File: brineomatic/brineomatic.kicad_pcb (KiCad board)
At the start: 4 copper layers, 106 x 66.5 mm, 171 parts, among them J1 Conn_01x04_MountingPin, J10 5.08MM, J12 3.5MM, J14 3.5MM, J16 3.5MM, J19 USB_TYPE_C_16PIN, J21 Conn_01x04, J7 3.5MM, Q1 AO3400A, Q2 AO3400A, Q3 20N06, Q4 AO3400A, Q5 AO3400A, Q6 AO3400A, Q7 FDC6330L, Q8 S8050, Q9 S8050, SW1 RESET, SW2 BOOT, U1 ADS1115IDGSR, U2 LM74700, U3 XL1509-5.0, U4 ESP32-S3-WROOM-1-N16R8, U5 USBLC6-2SC6, U6 XC6210B332MR, U7 CH334F, U8 CH343P, U9 TMC2209-LA, Y1 12Mhz, Y2 32.768kHz

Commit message: added rs485 circuit
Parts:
- added C45: 10uF, Capacitor_SMD:C_0603_1608Metric, F.Cu at (109.6, 117.1)
- added C46: 100nF, Capacitor_SMD:C_0603_1608Metric, F.Cu at (109.6, 114.6)
- added J22: 3.5mm, Connector_Phoenix_MC:PhoenixContact_MC_1,5_3-G-3.5_1x03_P3.50mm_Horizontal, F.Cu at (111.0, 120.9)
- added R53: 10k, Resistor_SMD:R_0603_1608Metric, F.Cu at (109.6, 112.1)
- added R54: 10k, Resistor_SMD:R_0603_1608Metric, F.Cu at (109.6, 109.6)
- added R55: 10k, Resistor_SMD:R_0603_1608Metric, F.Cu at (114.2, 109.3)
- added R56: 10k, Resistor_SMD:R_0603_1608Metric, F.Cu at (119.0, 109.6)
- added R57: 10k, Resistor_SMD:R_0603_1608Metric, F.Cu at (119.0, 112.1)
- added R58: 120R, Resistor_SMD:R_0603_1608Metric, F.Cu at (119.0, 114.6)
- added R59: 10k, Resistor_SMD:R_0603_1608Metric, F.Cu at (119.0, 117.1)
- added U10: MAX3485, Package_SO:SOIC-8_3.9x4.9mm_P1.27mm, F.Cu at (114.3, 114.1)
- renumbered D11 to D10, D10 to D11
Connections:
- U4 pad 24: /ESP32-S3/GPIO47 -> GPIO47
- U4 pad 25: /ESP32-S3/GPIO48 -> GPIO48
- U4 pad 5: /ESP32-S3/GPIO5 -> GPIO5

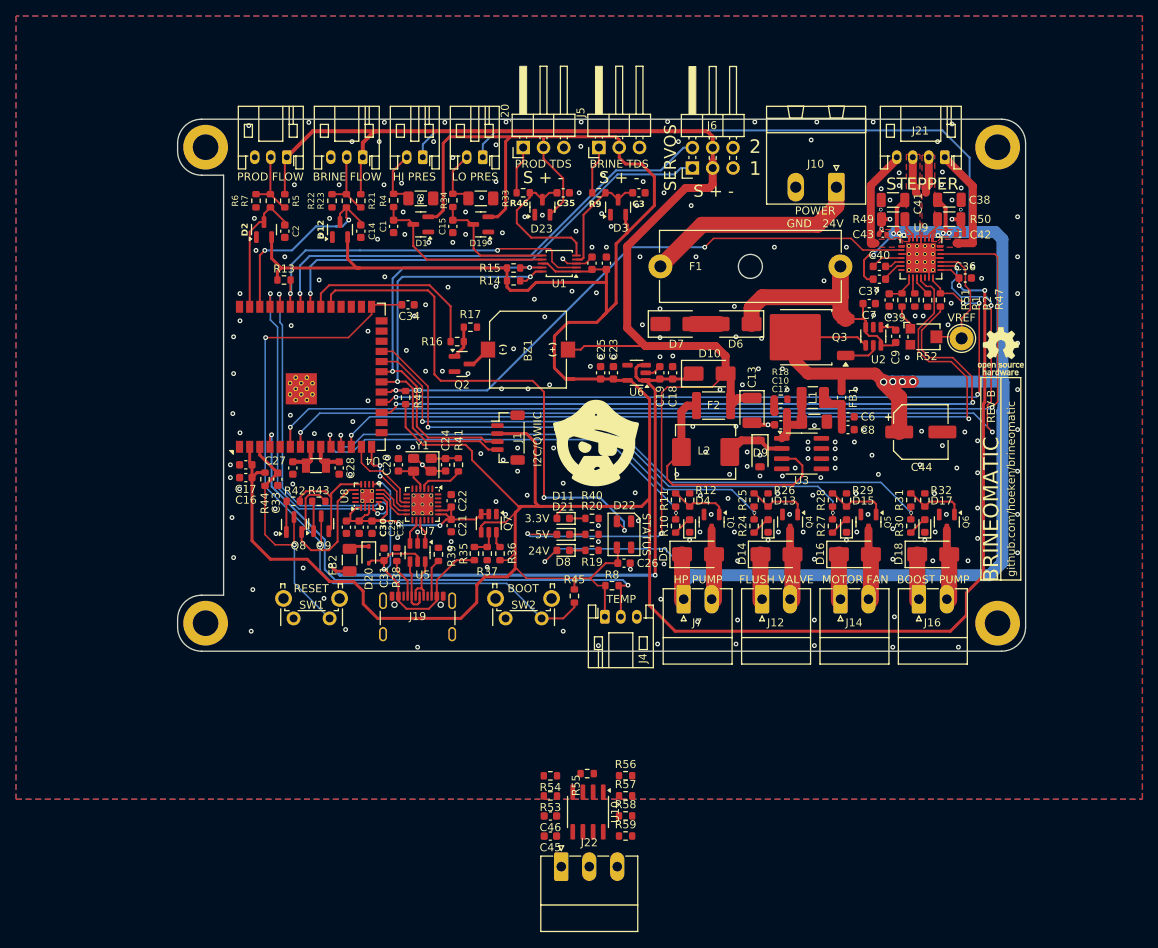
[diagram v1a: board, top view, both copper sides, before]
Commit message: stacked tds, removed stepper vref, pulled in esp32-s3 schematic, added extra relay output
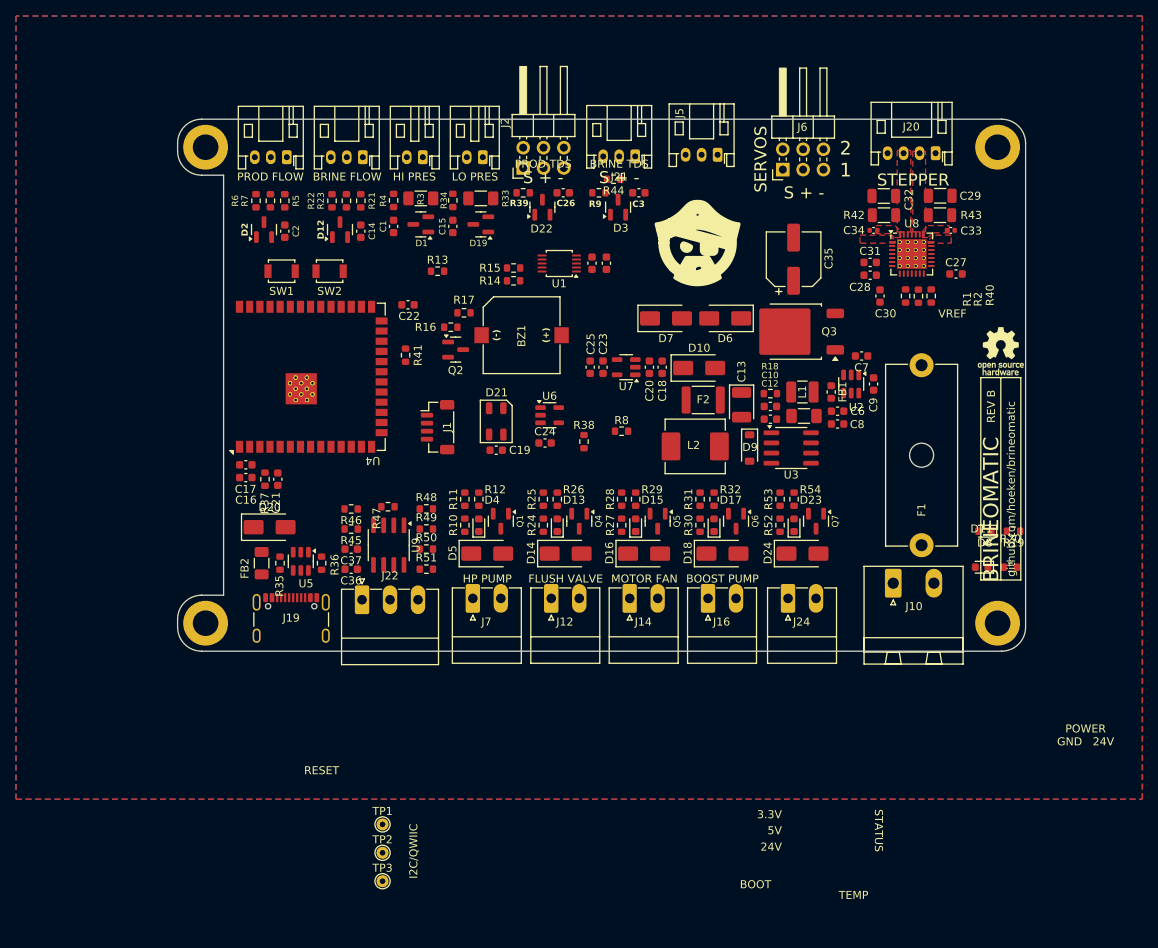
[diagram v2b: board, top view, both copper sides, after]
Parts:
- removed the C20 at (90.6, 70.7)
- removed the C21 at (97.2, 78.3)
- removed the C22 at (97.2, 75.2)
- removed the C27 at (77.4, 71.1)
- removed the C28 at (83.2, 71.1)
- removed the C29 at (85.7, 78.5)
- removed the C30 at (84.1, 78.5)
- removed the C31 at (88.8, 81.9)
- removed the C32 at (87.3, 78.5)
- removed the D21 at (111.2, 77.4)
- removed the J20 at (106.2, 31.0)
- removed the J5 at (115.7, 31.0)
- removed Q8, Q9: S8050, Package_TO_SOT_SMD:SOT-23
- removed the R35 at (100.1, 81.8)
- removed the R36 at (103.3, 81.8)
- removed the R37 at (101.7, 81.8)
- removed the R40 at (114.8, 77.4)
- removed the R41 at (98.1, 70.7)
- removed the R42 at (77.5, 75.3)
- removed the R43 at (80.7, 75.3)
- removed the R51 at (153.6, 50.1)
- removed the U7 at (93.6, 75.7)
- removed the U8 at (86.7, 74.6)
- removed Y1: 12Mhz, Crystal:Crystal_SMD_SeikoEpson_TSX3225-4Pin_3.2x2.5mm
- removed Y2: 32.768kHz, Crystal:Crystal_SMD_3215-2Pin_3.2x1.5mm
- added D23: RED, LED_SMD:LED_0603_1608Metric, F.Cu at (140.1, 78.2)
- added D24: SS54, Diode_SMD:D_SMA, F.Cu at (141.1, 81.8)
- added J2: ~, Connector_PinHeader_2.54mm:PinHeader_2x03_P2.54mm_Horizontal, F.Cu at (106.2, 33.6)
- added J21: ~, Connector_JST:JST_PH_S3B-PH-K_1x03_P2.00mm_Horizontal, F.Cu at (120.2, 32.1)
- added J24: 3.5MM, yarrboard:PhoenixContact_MC_1,5_2-G-3.5_1x02_P3.50mm_Horizontal, F.Cu at (139.3, 87.4)
- added R44: 4.7K, Resistor_SMD:R_0603_1608Metric, F.Cu at (117.5, 35.0)
- added R53: 100R, Resistor_SMD:R_0603_1608Metric, F.Cu at (138.3, 75.0)
- added R54: 10k, Resistor_SMD:R_0603_1608Metric, F.Cu at (140.1, 75.0)
- added TP2: ~, TestPoint:TestPoint_THTPad_D1.5mm_Drill0.7mm, F.Cu at (88.6, 119.2)
- added TP3: ~, TestPoint:TestPoint_THTPad_D1.5mm_Drill0.7mm, F.Cu at (88.6, 122.8)
- added U6: SN74LV1T34DBV, Package_TO_SOT_SMD:SOT-23-5, F.Cu at (109.5, 64.5)
- C24: value 15pF -> 100nF
- D20: value 1N5819WS -> SS36; footprint Diode_SMD:D_SOD-323 -> Diode_SMD:D_SMA
- FB2: value 1.5A -> 4A
- Q7: value FDC6330L -> AO3400A; footprint Package_TO_SOT_SMD:TSOT-23-6 -> Package_TO_SOT_SMD:SOT-23
- R52: value 20k -> 1k; footprint Potentiometer_SMD:Potentiometer_Bourns_TC33X_Vertical -> Resistor_SMD:R_0603_1608Metric
- SW1, SW2: footprint Button_Switch_THT:SW_Tactile_SPST_Angled_PTS645Vx58-2LFS -> Button_Switch_SMD:SW_SPST_B3U-1000P
- TP1: value TestPoint -> ~; footprint TestPoint:TestPoint_THTPad_D3.0mm_Drill1.5mm -> TestPoint:TestPoint_THTPad_D1.5mm_Drill0.7mm
- moved TP1 94.5 mm to (88.6, 115.7), turned to 0 degrees
- moved J5 59.4 mm to (130.5, 31.9), turned to 180 degrees
- moved D8 52.8 mm to (163.9, 79.0)
- moved R19 52.8 mm to (167.5, 79.0)
- moved D11 52.5 mm to (163.5, 83.5)
- moved R20 52.5 mm to (167.1, 83.5)
- moved SW2 50.9 mm to (82.0, 46.5)
- moved J10 50.0 mm to (152.5, 85.5), turned to 0 degrees
- moved F1 47.8 mm to (156.0, 80.8), turned to 90 degrees
- moved SW1 43.8 mm to (76.0, 46.5)
- moved C36 41.6 mm to (84.7, 83.8)
- moved R45 41.6 mm to (84.7, 78.7)
- moved R46 41.6 mm to (84.7, 76.2)
- moved R47 41.6 mm to (89.3, 75.9)
- moved R49 41.6 mm to (94.1, 78.7)
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- renumbered C26 to C19, C19 to C20, C33 to C21, C34 to C22, C35 to C26, C36 to C27, C37 to C28, C38 to C29, C39 to C30, C40 to C31, C41 to C32, C42 to C33, C43 to C34, C44 to C35, C45 to C36, C46 to C37, D22 to D21, D23 to D22, J21 to J20, J2 to J3, J3 to J4, J4 to J5, R38 to R35, R39 to R36, R44 to R37, R45 to R38, R46 to R39, R47 to R40, R48 to R41, R49 to R42, R50 to R43, R53 to R45, R54 to R46, R55 to R47, R56 to R48, R57 to R49, R58 to R50, R59 to R51, U6 to U7, U9 to U8, U10 to U9
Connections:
- net ADC_ALERT/RDY renamed ADC_ALERT
- C13 pad 1: Net-(D10-A) -> 5V_TRUE
- C18 pad 1: ESP32_5V -> +5V
- C19 pad 1: +3.3V -> +5V
- C20 pad 1: ESP32_5V -> +5V
- C24 pad 1: Net-(C24-Pad1) -> +5V
- D10 pad 2: Net-(D10-A) -> 5V_TRUE
- D21 pad 1: +3.3V -> +5V
- D21 pad 4: /ESP32-S3/GPIO38 -> Net-(D21-DIN)
- F2 pad 1: Net-(D10-A) -> 5V_TRUE
- FB2 pad 2: ESP32_5V -> +5V
- J11 pad 1: +5V -> 5V_TRUE
- J4 pad 1: +5V -> 5V_TRUE
- J6 pad 3: +5V -> 5V_TRUE
- J6 pad 4: +5V -> 5V_TRUE
- Q7 pad 1: GND -> Net-(Q7-G)
- Q7 pad 2: /ESP32-S3/3.3VUSB -> GND
- Q7 pad 3: /ESP32-S3/3.3VUSB -> Net-(D24-A)
- R16 pad 2: /ESP32-S3/GPIO39 -> /Piezo/PIEZO
- R21 pad 2: +5V -> 5V_TRUE
- R39 pad 1: Net-(J20-Pin_1) -> PRODUCT_TDS
- R5 pad 2: +5V -> 5V_TRUE
- R52 pad 2: /Stepper Driver/VREF -> /Solenoid Driver 5/INPUT
- R9 pad 1: Net-(J5-Pin_1) -> BRINE_TDS
- TP1 pad 1: /Stepper Driver/VREF -> /ESP32-S3/EN
- U4 pad 8: /ESP32-S3/GPIO15_RTC -> /ESP32-S3/GPIO15
- U4 pad 9: /ESP32-S3/GPIO16_RTC -> /ESP32-S3/GPIO16
- U5 pad 1: /ESP32-S3/HUB_D+ -> /ESP32-S3/ESP_USB+
- U5 pad 3: /ESP32-S3/HUB_D- -> /ESP32-S3/ESP_USB-
- U7 pad 1: ESP32_5V -> +5V
- U7 pad 3: ESP32_5V -> +5V
- U8 pad 17: /Stepper Driver/VREF -> unconnected-(U8-VREF-Pad17)
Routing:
- net +3.3V: track 444.4 -> 0.00 mm, vias 2 -> 0
- net +24V: track 309.0 -> 0.00 mm, vias 12 -> 0
- net +5V: track 178.3 -> 0.00 mm, vias 2 -> 0
- net TMC2209_DIR: track 117.6 -> 0.00 mm, vias 2 -> 0
- net TMC2209_STEP: track 117.5 -> 0.00 mm, vias 4 -> 0
- net TMC2209_DIAG: track 103.5 -> 0.00 mm, vias 2 -> 0
- net TMC2209_TX: track 94.2 -> 0.00 mm, vias 4 -> 0
- net TMC2209_RX: track 92.1 -> 0.00 mm, vias 2 -> 0
- net /ESP32-S3/GPIO0_BOOT: track 90.0 -> 0.00 mm, vias 2 -> 0
- net SOLENOID4: track 78.2 -> 0.00 mm, vias 2 -> 0
- net ESP32_5V: track 77.6 -> 0.00 mm, vias 2 -> 0
- net TMC2209_EN: track 74.8 -> 0.00 mm, vias 2 -> 0
- net SOLENOID3: track 70.2 -> 0.00 mm, vias 2 -> 0
- net /ESP32-S3/GPIO38: track 66.4 -> 0.00 mm, vias 2 -> 0
- net /ESP32-S3/GPIO4: track 65.1 -> 0.00 mm, vias 2 -> 0
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
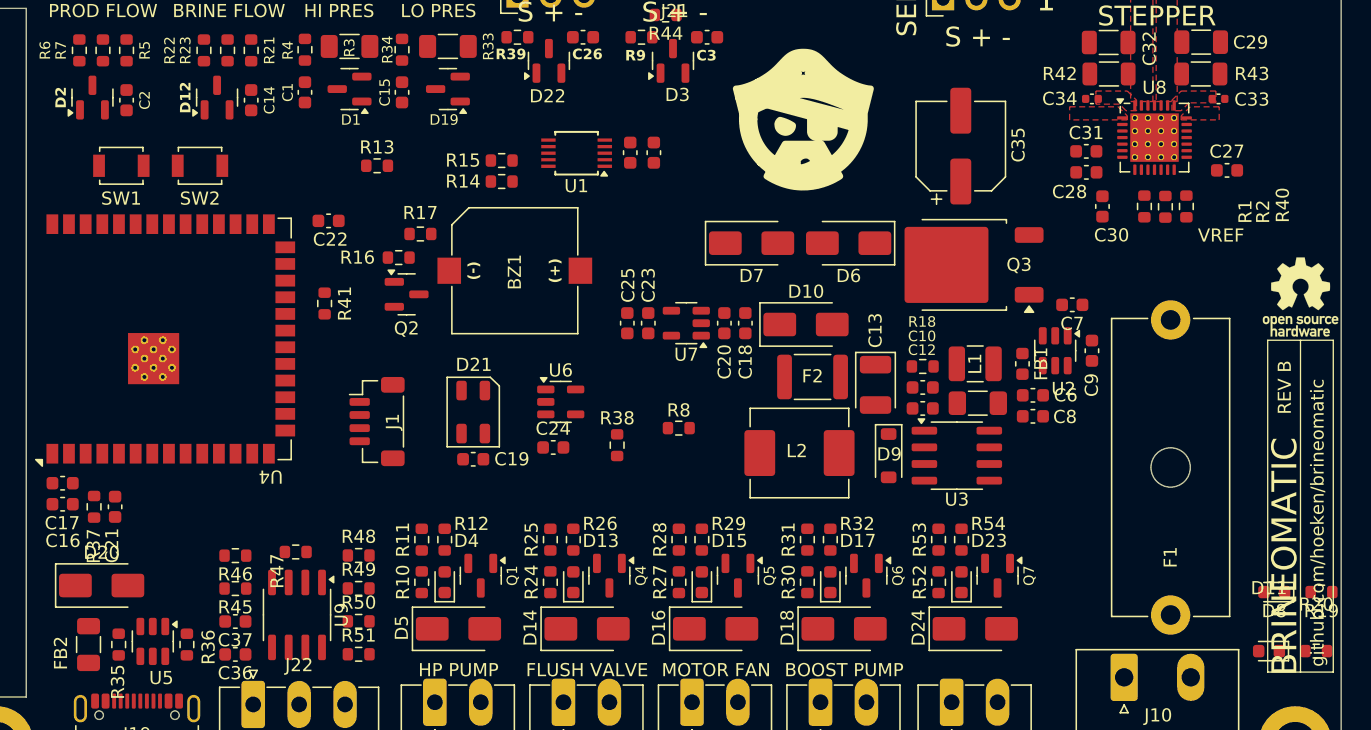
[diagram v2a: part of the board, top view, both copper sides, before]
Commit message: added sendit piezo
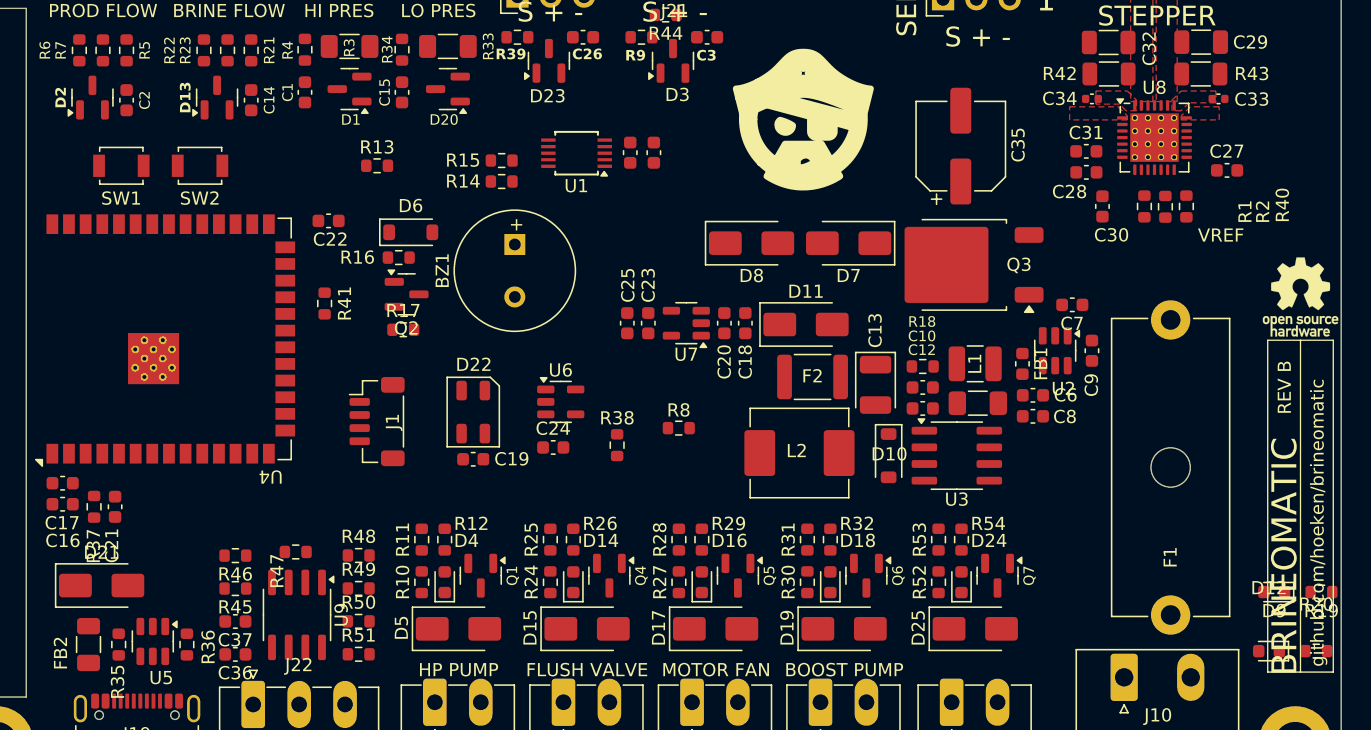
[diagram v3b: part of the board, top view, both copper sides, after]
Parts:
- added D6: B5819W, Diode_SMD:D_SOD-123, F.Cu at (98.1, 51.6)
- BZ1: footprint yarrboard:Buzzer_FUET_9.6x9.6 -> yarrboard:MagneticBuzzer_QMB-09B-03
- moved R17 7.41 mm to (97.5, 59.0), turned to 0 degrees
- renumbered D9 to D10, D10 to D11, D11 to D12, D12 to D13, D13 to D14, D14 to D15, D15 to D16, D16 to D17, D17 to D18, D18 to D19, D19 to D20, D20 to D21, D21 to D22, D22 to D23, D23 to D24, D24 to D25, D6 to D7, D7 to D8, D8 to D9
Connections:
- BZ1 pad 1: +5V -> +3.3V
- R17 pad 1: GND -> Net-(Q2-G)
- R17 pad 2: Net-(Q2-G) -> GND

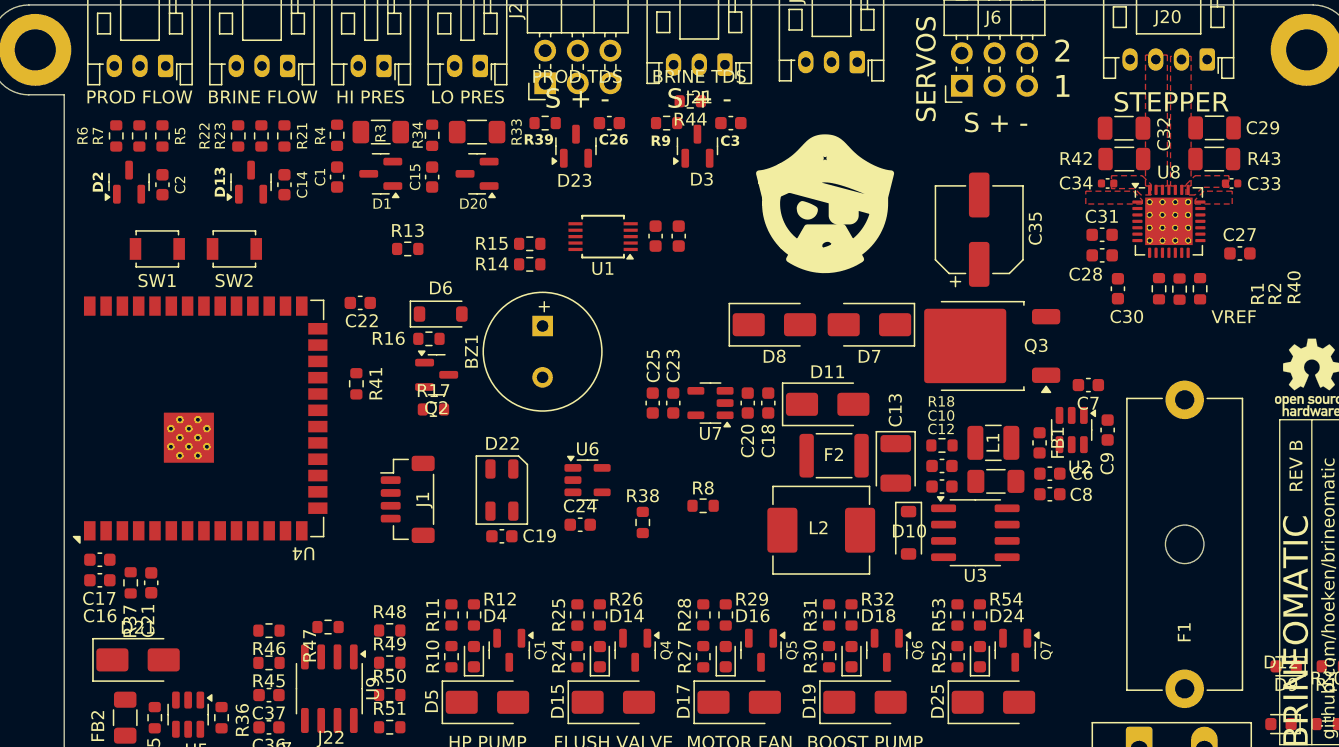
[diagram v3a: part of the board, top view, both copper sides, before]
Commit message: worked on component layout a bit more.
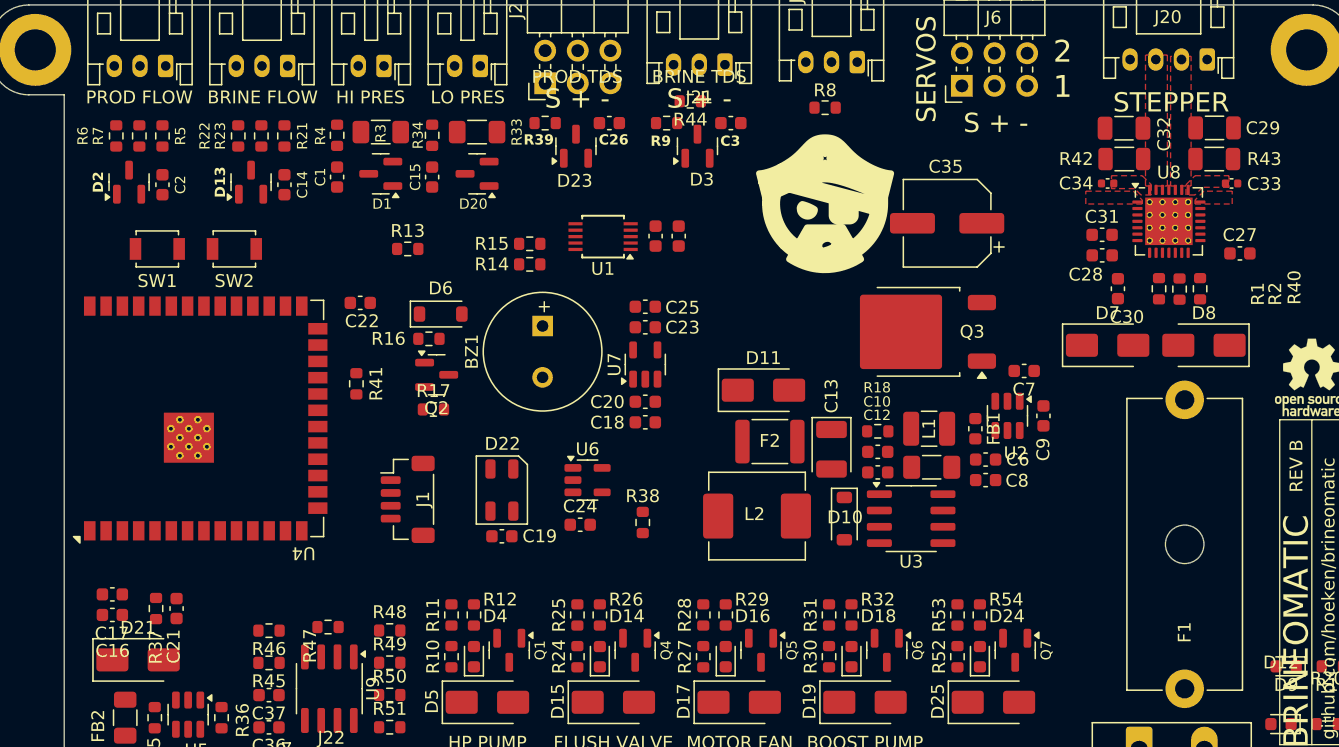
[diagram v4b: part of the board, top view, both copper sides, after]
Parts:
- moved D8 33.5 mm to (157.5, 54.0), turned to 180 degrees
- moved R8 32.4 mm to (128.0, 35.5)
- moved D7 18.6 mm to (150.0, 54.0), turned to 0 degrees
- moved C18 9.69 mm to (114.0, 60.0), turned to 0 degrees
- moved C20 7.98 mm to (114.0, 58.4), turned to 0 degrees
- moved C25 7.52 mm to (114.0, 51.0), turned to 0 degrees
- moved C23 6.29 mm to (114.0, 52.6), turned to 0 degrees
- moved U7 5.90 mm to (114.0, 55.5), turned to 90 degrees
- moved L2 5.12 mm to (122.7, 67.3)
- moved C10 5.12 mm to (132.1, 62.3)
- moved C12 5.12 mm to (132.1, 63.9)
- moved C13 5.12 mm to (128.5, 62.1)
- moved C6 5.12 mm to (140.5, 62.9)
- moved C7 5.12 mm to (143.5, 56.0)
- moved C9 5.12 mm to (145.0, 59.5)
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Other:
- board text removed: "VREF"
